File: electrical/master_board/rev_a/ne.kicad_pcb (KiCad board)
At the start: 2 copper layers, 42.2 x 39 mm, 1 part, among them CN60 HCSR04;F1x4H

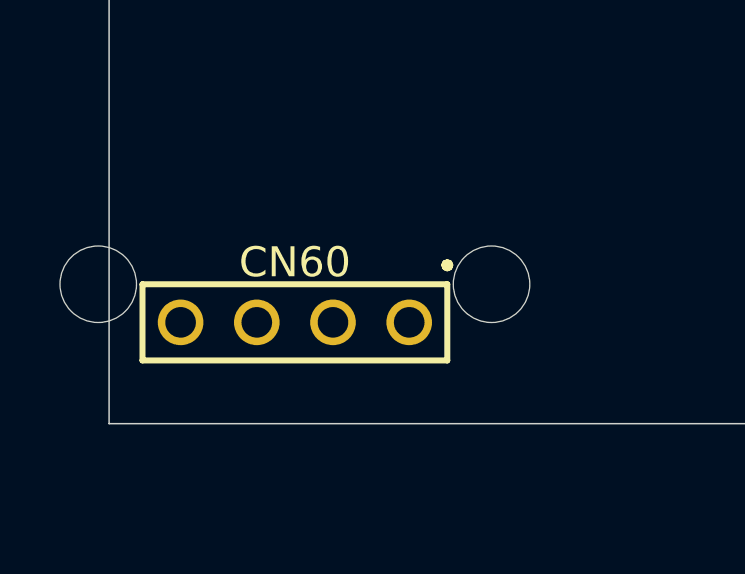
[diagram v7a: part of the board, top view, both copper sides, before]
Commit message: Manually put CN60 on the back surface; need to get softare capable of doing the same.
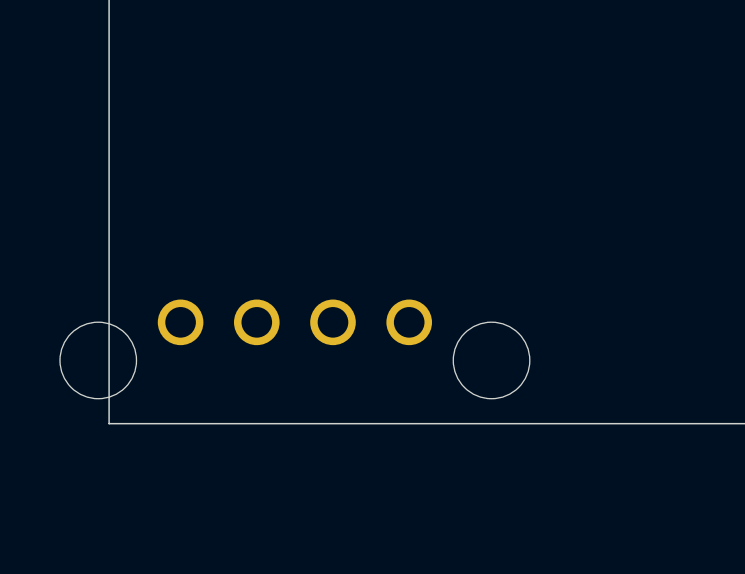
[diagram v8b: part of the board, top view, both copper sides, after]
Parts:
- CN60: moved to B.Cu
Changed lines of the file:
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@@
     (uvia_dia 0.3)
     (uvia_drill 0.1)
-    (add_net "Net-(CN60-Pad1)")
-    (add_net "Net-(CN60-Pad2)")
-    (add_net "Net-(CN60-Pad3)")
-    (add_net "Net-(CN60-Pad4)")
   )
-  (module HR2:HCSR04_F1x4H (layer F.Cu)
+  (module HR2:HCSR04_F1x4H (layer B.Cu)
     (at 136.1937 57.6226)
-    (fp_text reference CN60 (at 0 -2) (layer F.SilkS)
-      (effects (font (size 1 1) (thickness 0.2)))
+    (fp_text reference CN60 (at 0 2) (layer B.SilkS)
+      (effects (font (size 1 1) (thickness 0.2)) (justify mirror))
     )
-    (fp_text value HCSR04;F1x4H (at 0 0) (layer F.Fab)
-      (effects (font (size 1 1) (thickness 0.2)))
+    (fp_text value HCSR04;F1x4H (at 0 0) (layer B.Fab)
+      (effects (font (size 1 1) (thickness 0.2)) (justify mirror))
     )
-    (fp_line (start 5.08 -1.27) (end 5.08 1.27) (layer F.SilkS) (width 0.2))
-    (fp_line (start 5.08 1.27) (end -5.08 1.27) (layer F.SilkS) (width 0.2))
-    (fp_line (start -5.08 1.27) (end -5.08 -1.27) (layer F.SilkS) (width 0.2))
-    (fp_line (start -5.08 -1.27) (end 5.08 -1.27) (layer F.SilkS) (width 0.2))
-    (fp_line (start 5.18 -1.91) (end 5.15 -1.98) (layer F.SilkS) (width 0.2))
-    (fp_line (start 5.15 -1.98) (end 5.08 -2) (layer F.SilkS) (width 0.2))
-    (fp_line (start 5.08 -2) (end 5.01 -1.98) (layer F.SilkS) (width 0.2))
-    (fp_line (start 5.01 -1.98) (end 4.98 -1.91) (layer F.SilkS) (width 0.2))
-    (fp_line (start 4.98 -1.91) (end 5.01 -1.83) (layer F.SilkS) (width 0.2))
-    (fp_line (start 5.01 -1.83) (end 5.08 -1.8) (layer F.SilkS) (width 0.2))
-    (fp_line (start 5.08 -1.8) (end 5.15 -1.83) (layer F.SilkS) (width 0.2))
-    (fp_line (start 5.15 -1.83) (end 5.18 -1.91) (layer F.SilkS) (width 0.2))
-    (pad "HCSR04 West Tie Down Hole" np_thru_hole circle (at -6.555 -1.27) (size 2.55 2.55) (drill 2.55) (layers *.Cu *.Mask))
-    (pad "HCSR04 East Tie Down Hole" np_thru_hole circle (at 6.555 -1.27) (size 2.55 2.55) (drill 2.55) (layers *.Cu *.Mask))
+    (fp_line (start 5.08 1.27) (end 5.08 -1.27) (layer B.SilkS) (width 0.2))
+    (fp_line (start 5.08 -1.27) (end -5.08 -1.27) (layer B.SilkS) (width 0.2))
+    (fp_line (start -5.08 -1.27) (end -5.08 1.27) (layer B.SilkS) (width 0.2))
+    (fp_line (start -5.08 1.27) (end 5.08 1.27) (layer B.SilkS) (width 0.2))
+    (fp_line (start 5.18 1.91) (end 5.15 1.98) (layer B.SilkS) (width 0.2))
+    (fp_line (start 5.15 1.98) (end 5.08 2) (layer B.SilkS) (width 0.2))
+    (fp_line (start 5.08 2) (end 5.01 1.98) (layer B.SilkS) (width 0.2))
+    (fp_line (start 5.01 1.98) (end 4.98 1.91) (layer B.SilkS) (width 0.2))
+    (fp_line (start 4.98 1.91) (end 5.01 1.83) (layer B.SilkS) (width 0.2))
+    (fp_line (start 5.01 1.83) (end 5.08 1.8) (layer B.SilkS) (width 0.2))
+    (fp_line (start 5.08 1.8) (end 5.15 1.83) (layer B.SilkS) (width 0.2))
+    (fp_line (start 5.15 1.83) (end 5.18 1.91) (layer B.SilkS) (width 0.2))
+    (pad "HCSR04 West Tie Down Hole" np_thru_hole circle (at -6.555 1.27) (size 2.55 2.55) (drill 2.55) (layers *.Cu *.Mask))
+    (pad "HCSR04 East Tie Down Hole" np_thru_hole circle (at 6.555 1.27) (size 2.55 2.55) (drill 2.55) (layers *.Cu *.Mask))
     (pad 4 thru_hole circle (at -3.81 0) (size 1.52 1.52) (drill 1.02) (layers *.Cu *.Mask))
     (pad 3 thru_hole circle (at -1.27 0) (size 1.52 1.52) (drill 1.02) (layers *.Cu *.Mask))
